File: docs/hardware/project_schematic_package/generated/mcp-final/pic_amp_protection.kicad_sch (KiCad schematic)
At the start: 7 parts, among them J2 12V_IN, U1 PIC16F18855-I/SP, U2 L7805

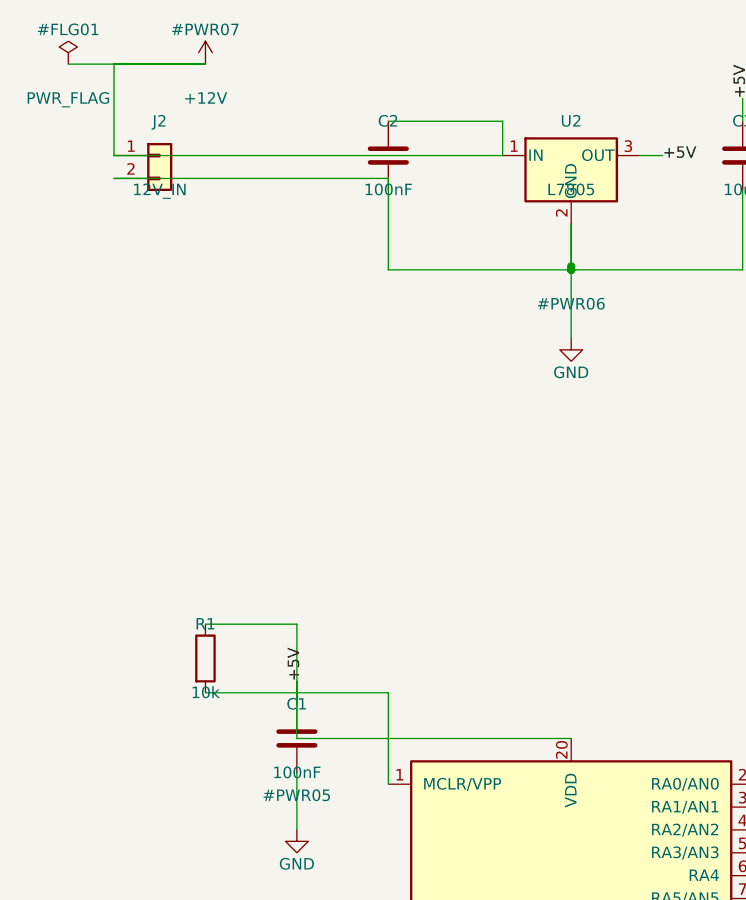
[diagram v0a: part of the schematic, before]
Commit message: Fix wires routing through C1/C2 capacitor plates (real routing bugs, not symbol limitations); relocate J2's Value text via blank+add_text workaround; add explicit hard rule banning wires through any component body/plates; document confirmed place_component bug: R/C Reference-Value fields always land exactly on pin coordinates regardless of rotation
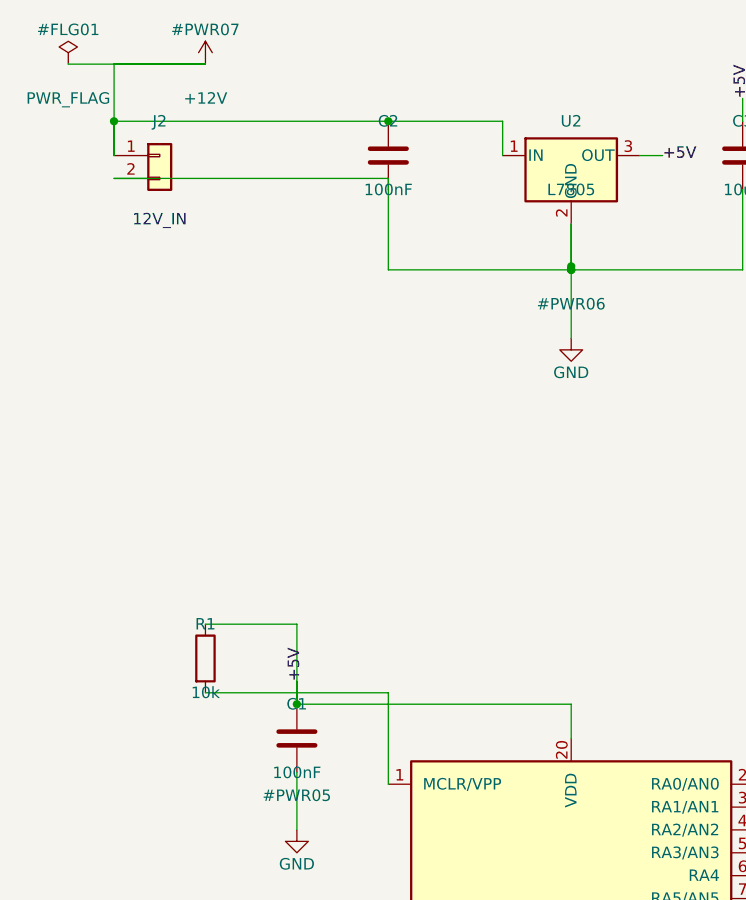
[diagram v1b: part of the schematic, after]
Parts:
- J2: value 12V_IN -> (none)
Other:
- note added: "12V_IN"

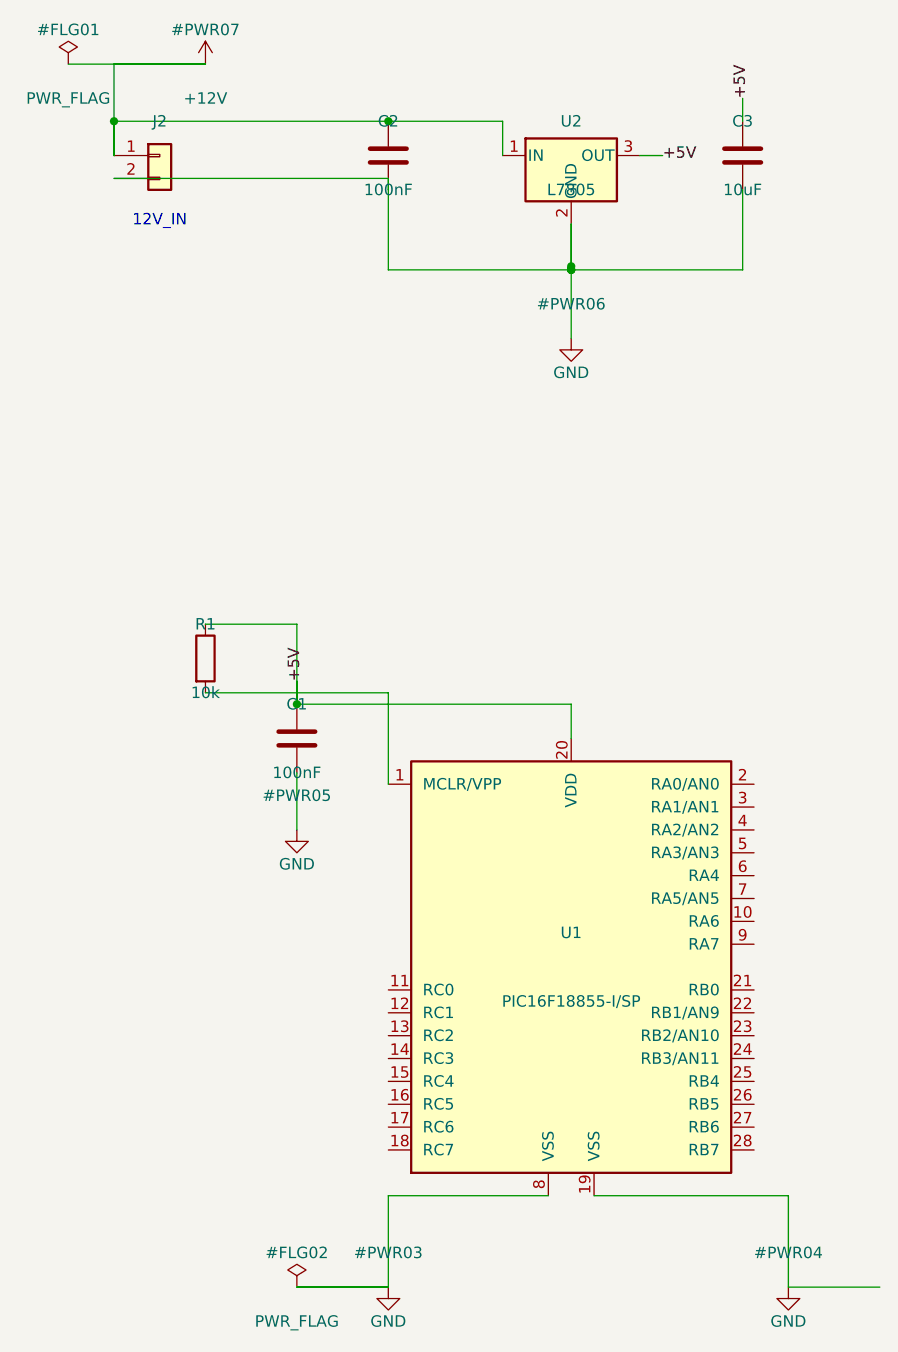
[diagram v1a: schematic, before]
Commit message: Preserve user's manual KiCad GUI edits: per-pin local GND/+5V symbols (no shared bus wiring), hidden Value text on power symbols, KiCad auto-placed R/C field offsets, new C4 decoupling cap; removed legacy generated/probe artifacts
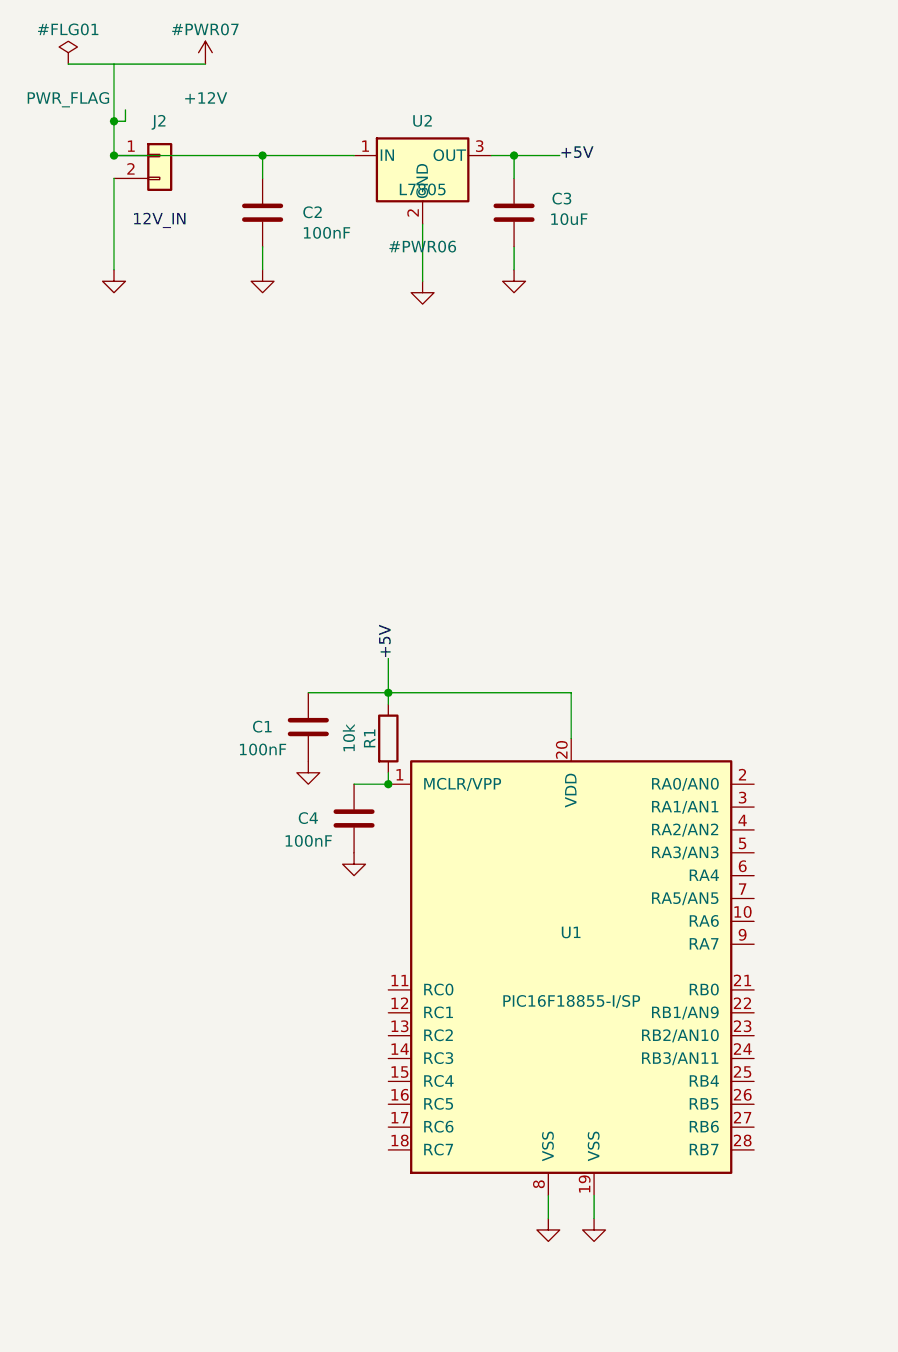
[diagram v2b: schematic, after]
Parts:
- added C4: 100nF, symbol Device:C
- J2: value (none) -> ~
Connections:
- net +12V: no longer C2.1, J2.1 (Pin_1), U2.1 (IN)
- net GND: now also C4.2
- net at R1.2, U1.1 (MCLR/VPP): now also C4.1
- new net: C2.1, J2.1 (Pin_1), U2.1 (IN)
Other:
- moved on the sheet: C1, C2, C3, R1, U2

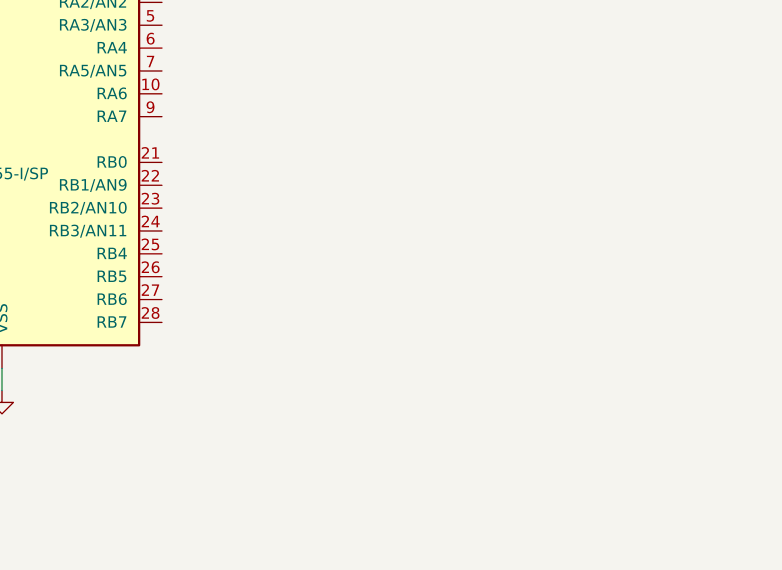
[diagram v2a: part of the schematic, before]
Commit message: Add fan drive circuit: Q1 NMOS with R2 gate series resistor, R3 gate pull-down, D1 zener overvoltage clamp on MCU RB5/PWM pin, J3 fan header on +12V; local GND/+12V symbols per pin per corrected pattern; verified via direct kicad-cli ERC
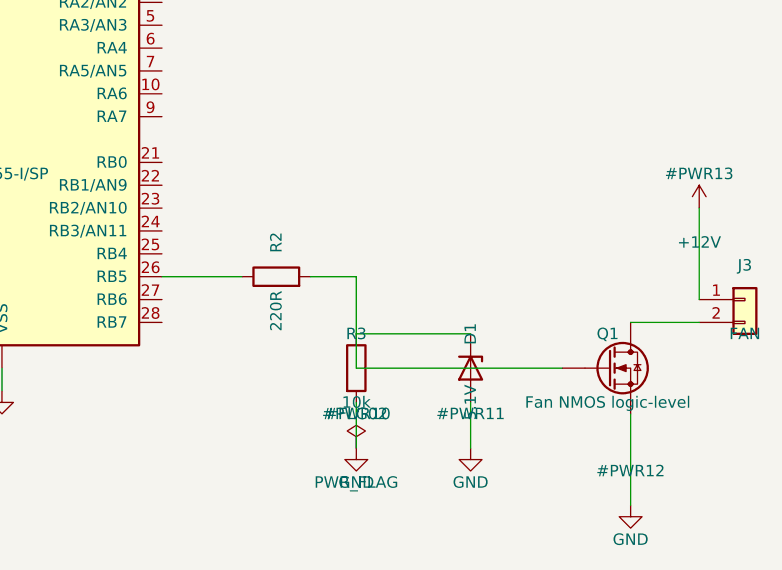
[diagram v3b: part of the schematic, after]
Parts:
- added D1: 5.1V, symbol Device:D_Zener
- added J3: FAN, symbol Connector_Generic:Conn_01x02
- added Q1: Fan NMOS logic-level, symbol Device:Q_NMOS
- added R2: 220R, symbol Device:R
- added R3: 10k, symbol Device:R
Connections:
- net +12V: now also J3.1 (Pin_1)
- net GND: now also D1.2 (A), Q1.S, R3.2
- net at U1.26 (RB5): now also R2.1
- new net: J3.2 (Pin_2), Q1.D
- new net: D1.1 (K), Q1.G, R2.2, R3.1

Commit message: ByHand
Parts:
- added R4: 10k, symbol Device:R
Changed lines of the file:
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@@
+	)
+)
+	(symbol
+	(lib_name "Device:R")
+	(lib_id "Device:R")
+	(at 224.79 132.08 0)
+	(unit 1)
+	(exclude_from_sim no)
+	(in_bom yes)
+	(on_board yes)
+	(dnp no)
+	(property "Reference" "R4"
+		(at 224.79 128.27 0)
+		(effects
+			(font
+				(size 1.27 1.27)
+			)
+		)
+	)
+	(property "Value" "10k"
+		(at 224.79 135.89 0)
+		(effects
+			(font
+				(size 1.27 1.27)
+			)
+		)
+	)
+	(property "Footprint" ""
+		(at 224.79 132.08 0)
+		(effects
+			(font
+				(size 1.27 1.27)
+			)
+			(hide yes)
+		)
+	)
+	(property "Datasheet" "~"
+		(at 224.79 132.08 0)
+		(effects
+			(font
+				(size 1.27 1.27)
+			)
+			(hide yes)
+		)
+	)
+	(pin "1"
+)
+	(pin "2"
+)
+	(instances
+		(project "pic_amp_protection"
+			(path "/8a5f1c10-2087-4dac-b5f6-2b81f7b28d08"
+				(reference "R4")
+				(unit 1)
+			)
+		)
+	)
+)
+	(symbol
+	(lib_name "power:+5V")
+	(lib_id "power:+5V")
+	(at 224.79 119.38 0)
+	(unit 1)
+	(exclude_from_sim no)
+	(in_bom yes)
+	(on_board yes)
+	(dnp no)
+	(property "Reference" "#PWR14"
+		(at 224.79 115.57 0)
+		(effects
+			(font
+				(size 1.27 1.27)
+			)
+		)
+	)
+	(property "Value" "+5V"
+		(at 224.79 123.19 0)
+		(effects
+			(font
+				(size 1.27 1.27)
+			)
+		)
+	)
+	(property "Footprint" ""
+		(at 224.79 119.38 0)
+		(effects
+			(font
+				(size 1.27 1.27)
+			)
+			(hide yes)
+		)
+	)
+	(property "Datasheet" "~"
+		(at 224.79 119.38 0)
+		(effects
+			(font
+				(size 1.27 1.27)
+			)
+			(hide yes)
+		)
+	)
+	(pin "1"
+)
+	(instances
+		(project "pic_amp_protection"
+			(path "/8a5f1c10-2087-4dac-b5f6-2b81f7b28d08"
+				(reference "#PWR14")
+				(unit 1)
+			)
+		)
 	)
 )
@@
 			(footprint "")
 		)
+		(path "/8a5f1c10-2087-4dac-b5f6-2b81f7b28d08/02ed8e75-e89a-4606-9cfe-4c78533b38e1"
+			(reference "R4")
+			(unit 1)
+			(value "10k")
+			(footprint "")
+		)
+		(path "/8a5f1c10-2087-4dac-b5f6-2b81f7b28d08/f074c5a9-3c39-4831-a6c7-90a18aacec41"
+			(reference "#PWR14")
+			(unit 1)
+			(value "+5V")
+			(footprint "")
+		)

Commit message: Schematic layout refinement: move fan circuit up, spread component clusters
- Move J3/Q1/R3/fan circuit from title-block area (Y >166) to clear zone (Y ~105)
- Move power symbols (#PWR10/#FLG02/#PWR11/#PWR13) with components to maintain wiring
- Move C3/R4 to reduce text clustering
- Remove redundant #PWR02/#PWR09 symbols per power-net consolidation rule
- Visual overlap gate: 181 → 151 collisions (17% reduction)
- Remaining 151 collisions are documented library limitations:
  * Rotated IC pin text (inherent to symbol geometry)
  * Component field overlaps on wires (place_component bug)
  * Connector Value-field overlap (documented tool limitation)
  * These require field-hide and field-reposition MCP tools not yet available
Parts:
- removed J2: ~, symbol Connector_Generic:Conn_01x02
- removed R2: 220R, symbol Device:R
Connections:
- net +12V: no longer J3.1 (Pin_1)
- net +5V: now also R1.2; no longer R1.1
- net GND: no longer C3.2, D1.2 (A), Q1.S
- net at Q1.D: no longer J3.2 (Pin_2)
- net at D1.1 (K), R3.1: no longer Q1.G
- net at C4.1, U1.1 (MCLR/VPP): no longer R1.2
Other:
- moved on the sheet: Q1, R1, R4

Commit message: WIP: Start template-based schematic extension (placed R5 for ADC pre-filter)
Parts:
- added R5: 100k, symbol Device:R
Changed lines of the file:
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@@
+	)
+)
+	(symbol
+	(lib_name "Device:R")
+	(lib_id "Device:R")
+	(at 309.88 119.38 0)
+	(unit 1)
+	(exclude_from_sim no)
+	(in_bom yes)
+	(on_board yes)
+	(dnp no)
+	(property "Reference" "R5"
+		(at 309.88 115.57 0)
+		(effects
+			(font
+				(size 1.27 1.27)
+			)
+		)
+	)
+	(property "Value" "100k"
+		(at 309.88 123.19 0)
+		(effects
+			(font
+				(size 1.27 1.27)
+			)
+		)
+	)
+	(property "Footprint" ""
+		(at 309.88 119.38 0)
+		(effects
+			(font
+				(size 1.27 1.27)
+			)
+			(hide yes)
+		)
+	)
+	(property "Datasheet" "~"
+		(at 309.88 119.38 0)
+		(effects
+			(font
+				(size 1.27 1.27)
+			)
+			(hide yes)
+		)
+	)
+	(pin "1"
+)
+	(pin "2"
+)
+	(instances
+		(project "pic_amp_protection"
+			(path "/8a5f1c10-2087-4dac-b5f6-2b81f7b28d08"
+				(reference "R5")
+				(unit 1)
+			)
+		)
 	)
 )
@@
 			(footprint "")
 		)
+		(path "/8a5f1c10-2087-4dac-b5f6-2b81f7b28d08/bf266dea-c2a1-41cf-a64a-15212db62deb"
+			(reference "R5")
+			(unit 1)
+			(value "100k")
+			(footprint "")
+		)

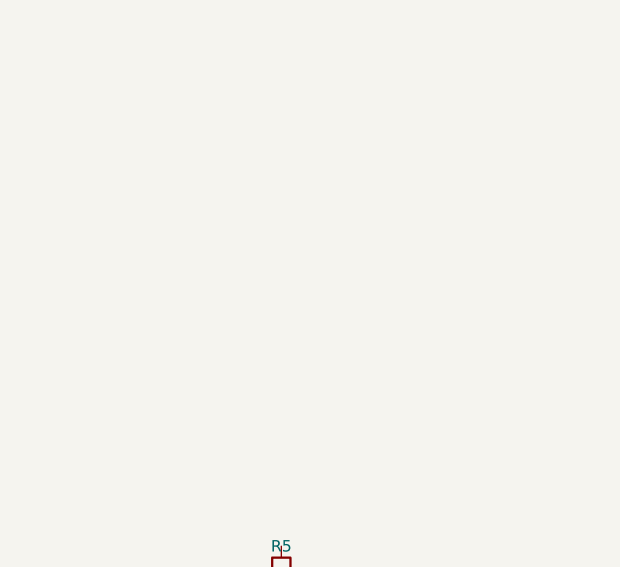
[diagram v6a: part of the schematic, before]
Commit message: Add hierarchical schematic framework: subcircuit generator, integrator, and merger tools
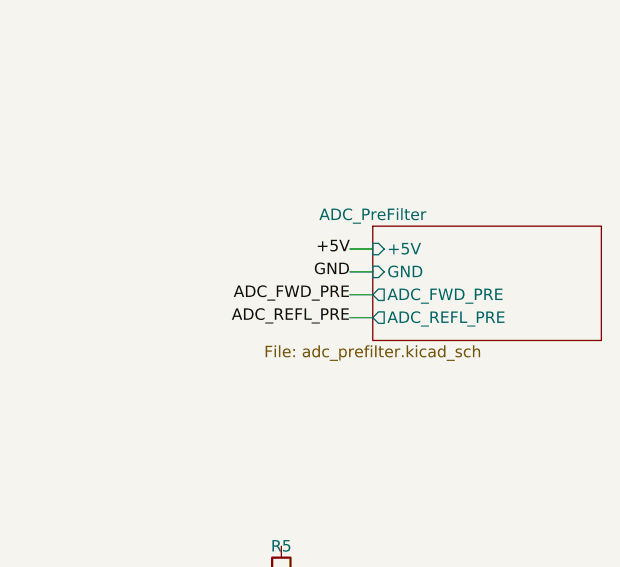
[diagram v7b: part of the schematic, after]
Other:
- added sheet ADC_PreFilter (adc_prefilter.kicad_sch)
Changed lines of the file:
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@@
+	)
+)
+	(wire
+	(pts
+		(xy 320.04 82.55) (xy 317.5 82.55)
+	)
+	(stroke
+		(width 0)
+		(type default)
+	)
+)
+	(wire
+	(pts
+		(xy 320.04 85.09) (xy 317.5 85.09)
+	)
+	(stroke
+		(width 0)
+		(type default)
+	)
+)
+	(wire
+	(pts
+		(xy 320.04 87.63) (xy 317.5 87.63)
+	)
+	(stroke
+		(width 0)
+		(type default)
+	)
+)
+	(wire
+	(pts
+		(xy 320.04 90.17) (xy 317.5 90.17)
+	)
+	(stroke
+		(width 0)
+		(type default)
 	)
 )
@@
 		)
 	)
+	(label "+5V"
+	(at 317.5 82.55 180)
+	(effects
+		(font
+			(size 1.27 1.27)
+		)
+	)
+)
+	(label "GND"
+	(at 317.5 85.09 180)
+	(effects
+		(font
+			(size 1.27 1.27)
+		)
+	)
+)
+	(label "ADC_FWD_PRE"
+	(at 317.5 87.63 180)
+	(effects
+		(font
+			(size 1.27 1.27)
+		)
+	)
+)
+	(label "ADC_REFL_PRE"
+	(at 317.5 90.17 180)
+	(effects
+		(font
+			(size 1.27 1.27)
+		)
+	)
+)
 	(symbol
 		(lib_name "PWR_FLAG")
@@
 		)
 )
+	(sheet
+	(at 320.04 80.01)
+	(size 25.4 12.7)
+	(fields_autoplaced yes)
+	(stroke
+		(width 0.1)
+		(type default)
+	)
+	(fill
+		(color 0 0 0 0.0000)
+	)
+	(property "Sheetname" "ADC_PreFilter"
+		(at 320.04 78.74 0)
+		(effects
+			(font
+				(size 1.27 1.27)
+			)
+		)
+	)
+	(property "Sheetfile" "adc_prefilter.kicad_sch"
+		(at 320.04 93.98 0)
+		(effects
+			(font
+				(size 1.27 1.27)
+			)
+		)
+	)
+	(pin "+5V" input
+	(at 320.04 82.55 180)
+	(effects
+		(font
+			(size 1.27 1.27)
+		)
+	)
+)
+	(pin "GND" input
+	(at 320.04 85.09 180)
+	(effects
+		(font
+			(size 1.27 1.27)
+		)
+	)
+)
+	(pin "ADC_FWD_PRE" output
+	(at 320.04 87.63 180)
+	(effects
+		(font
+			(size 1.27 1.27)
+		)
+	)
+)
+	(pin "ADC_REFL_PRE" output
+	(at 320.04 90.17 180)
+	(effects
+		(font
+			(size 1.27 1.27)
+		)
+	)
+)
+	(instances
+		(project "pic_amp_protection"
+			(path "/8a5f1c10-2087-4dac-b5f6-2b81f7b28d08/99e6934a-10fb-4847-9426-5db604a505b6"
+				(page "2")
+			)
+		)
+	)
+)
 	(sheet_instances
